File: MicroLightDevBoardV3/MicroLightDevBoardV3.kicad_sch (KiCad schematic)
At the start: 33 parts, among them J1 TYPE-C-31-M-12, J3 Conn_01x03_Socket, J4 Conn_01x01_Socket, J5 Conn_01x01_Socket, J6 Conn_01x04_Socket, SW1 SW_Push, U1 USBLC6-2P6, U2 STM32C071GBUx, U3 BQ25180, U4 S-85S1AB33-I6T1U, U7 MC3479

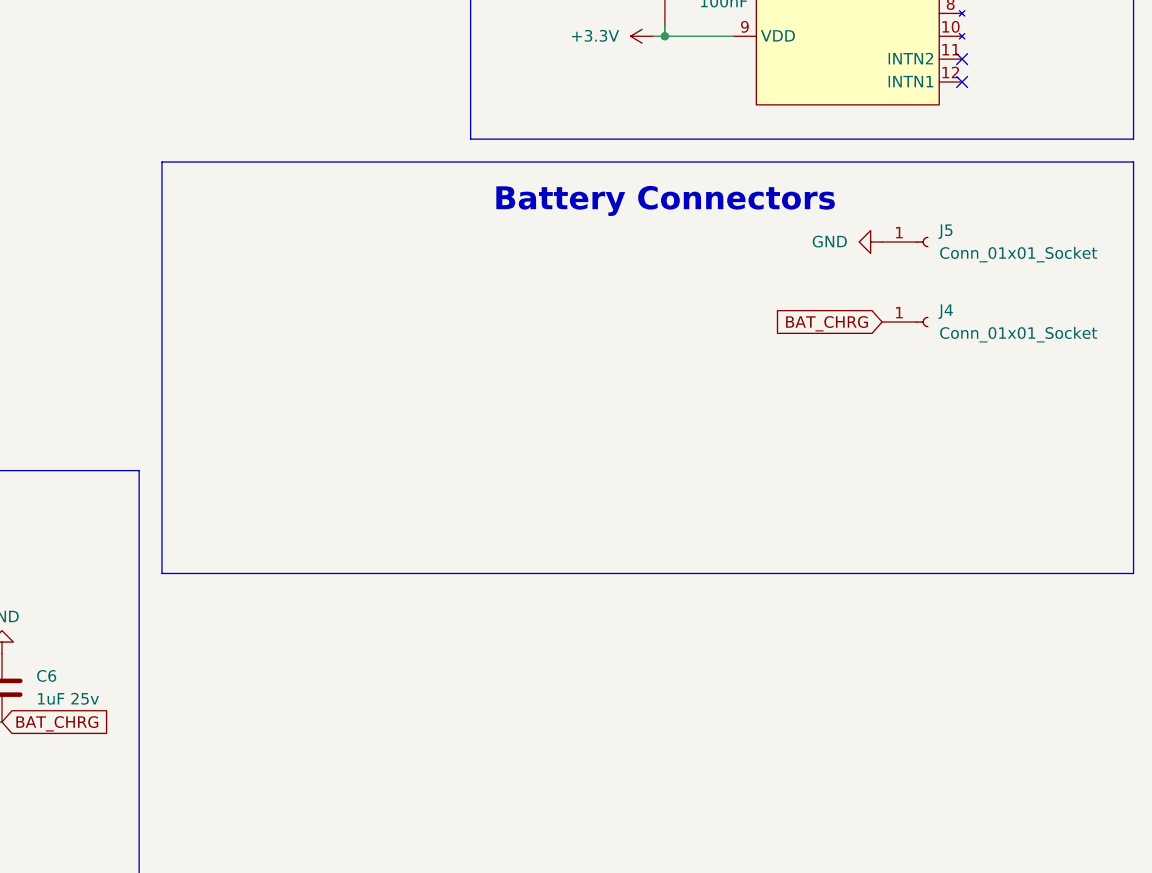
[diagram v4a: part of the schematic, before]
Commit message: add LCSC part numbers to schematic/pcb
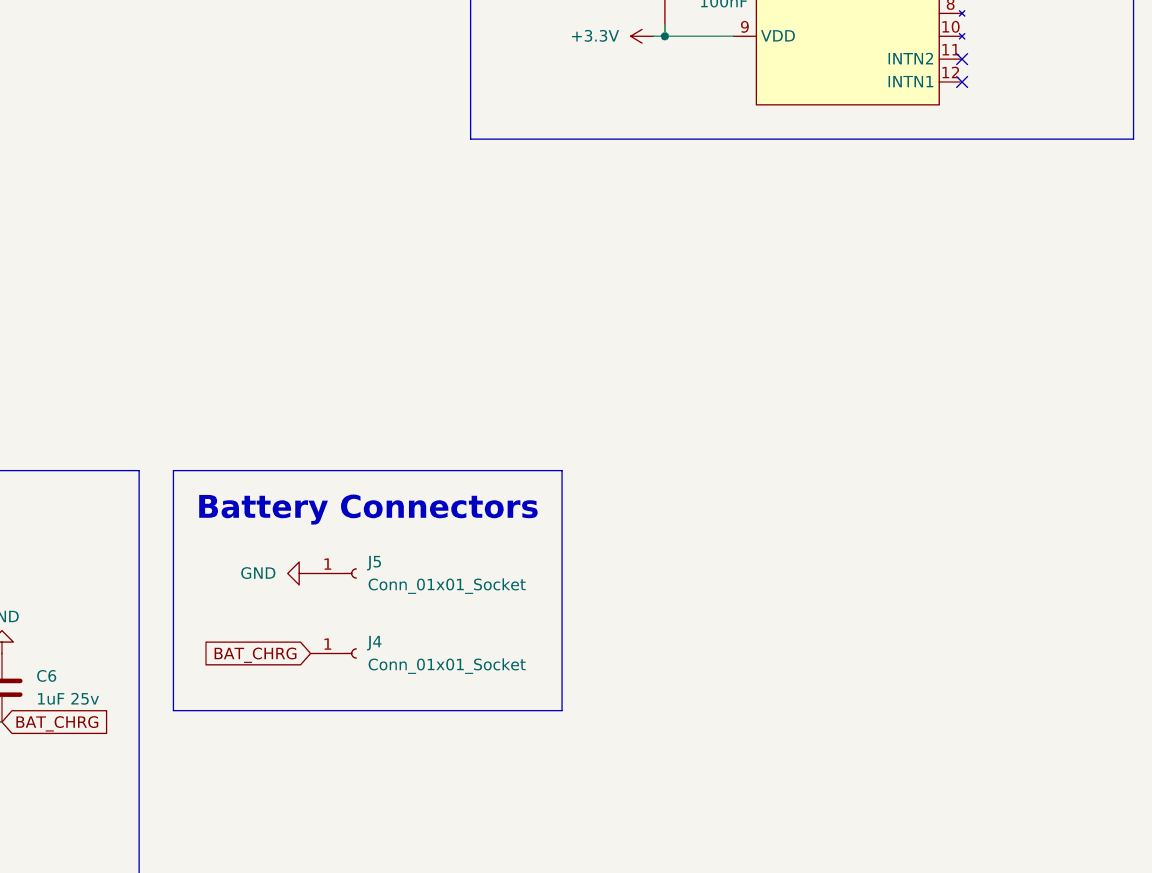
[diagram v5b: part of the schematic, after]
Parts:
- L1: LCSC (none) -> C92923; original_LCSC (none) -> C9900036204
- U4: LCSC (none) -> C7070110; LSCS C7070110 -> (none)
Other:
- moved on the sheet: J4, J5
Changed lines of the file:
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@@
 	)
 	(rectangle
-		(start 173.99 93.98)
-		(end 281.94 139.7)
+		(start 175.26 128.27)
+		(end 218.44 154.94)
 		(stroke
 			(width 0)
@@
 	(text "Battery Connectors"
 		(exclude_from_sim no)
-		(at 229.87 98.298 0)
+		(at 196.85 132.588 0)
 		(effects
 			(font
@@
 	(global_label "BAT_CHRG"
 		(shape input)
-		(at 254 111.76 180)
+		(at 190.5 148.59 180)
 		(fields_autoplaced yes)
 		(effects
@@
 		)
 		(property "Intersheetrefs" "${INTERSHEET_REFS}"
-			(at 241.5805 111.76 0)
+			(at 178.0805 148.59 0)
 			(effects
 				(font
@@
 	(symbol
 		(lib_id "Connector:Conn_01x01_Socket")
-		(at 259.08 111.76 0)
+		(at 195.58 148.59 0)
 		(unit 1)
 		(exclude_from_sim no)
@@
 		(fields_autoplaced yes)
 		(property "Reference" "J4"
-			(at 260.35 110.4899 0)
+			(at 196.85 147.3199 0)
 			(effects
 				(font
@@
 		)
 		(property "Value" "Conn_01x01_Socket"
-			(at 260.35 113.0299 0)
+			(at 196.85 149.8599 0)
 			(effects
 				(font
@@
 		)
 		(property "Footprint" "MicroLightDevBoard:battery_1x01_Vertical"
-			(at 259.08 111.76 0)
+			(at 195.58 148.59 0)
 			(effects
 				(font
@@
 		)
 		(property "Datasheet" "~"
-			(at 259.08 111.76 0)
+			(at 195.58 148.59 0)
 			(effects
 				(font
@@
 		)
 		(property "Description" "Generic connector, single row, 01x01, script generated"
-			(at 259.08 111.76 0)
+			(at 195.58 148.59 0)
 			(effects
 				(font
@@
 			)
 		)
-		(property "LSCS" "C7070110"
+		(property "LCSC" "C7070110"
 			(at 218.44 30.48 0)
 			(effects
@@
 	(symbol
 		(lib_id "Connector:Conn_01x01_Socket")
-		(at 259.08 102.87 0)
+		(at 195.58 139.7 0)
 		(unit 1)
 		(exclude_from_sim no)
@@
 		(fields_autoplaced yes)
 		(property "Reference" "J5"
-			(at 260.35 101.5999 0)
+			(at 196.85 138.4299 0)
 			(effects
 				(font
@@
 		)
 		(property "Value" "Conn_01x01_Socket"
-			(at 260.35 104.1399 0)
+			(at 196.85 140.9699 0)
 			(effects
 				(font
@@
 		)
 		(property "Footprint" "MicroLightDevBoard:battery_1x01_Vertical"
-			(at 259.08 102.87 0)
+			(at 195.58 139.7 0)
 			(effects
 				(font
@@
 		)
 		(property "Datasheet" "~"
-			(at 259.08 102.87 0)
+			(at 195.58 139.7 0)
 			(effects
 				(font
@@
 		)
 		(property "Description" "Generic connector, single row, 01x01, script generated"
-			(at 259.08 102.87 0)
+			(at 195.58 139.7 0)
 			(effects
 				(font
@@
 			)
 		)
+		(property "original_LCSC" "C9900036204"
+			(at 210.82 41.91 90)
+			(effects
+				(font
+					(size 1.27 1.27)
+				)
+				(hide yes)
+			)
+		)
+		(property "LCSC" "C92923"
+			(at 210.82 41.91 90)
+			(effects
+				(font
+					(size 1.27 1.27)
+				)
+				(hide yes)
+			)
+		)
 		(pin "2"
 		)
@@
 	(symbol
 		(lib_id "power:GND")
-		(at 254 102.87 270)
+		(at 190.5 139.7 270)
 		(unit 1)
 		(exclude_from_sim no)
@@
 		(fields_autoplaced yes)
 		(property "Reference" "#PWR024"
-			(at 247.65 102.87 0)
+			(at 184.15 139.7 0)
 			(effects
 				(font
@@
 		)
 		(property "Value" "GND"
-			(at 250.19 102.8699 90)
+			(at 186.69 139.6999 90)
 			(effects
 				(font
@@
 		)
 		(property "Footprint" ""
-			(at 254 102.87 0)
+			(at 190.5 139.7 0)
 			(effects
 				(font
@@
 		)
 		(property "Datasheet" ""
-			(at 254 102.87 0)
+			(at 190.5 139.7 0)
 			(effects
 				(font
@@
 		)
 		(property "Description" "Power symbol creates a global label with name \"GND\" , ground"
-			(at 254 102.87 0)
+			(at 190.5 139.7 0)
 			(effects
 				(font

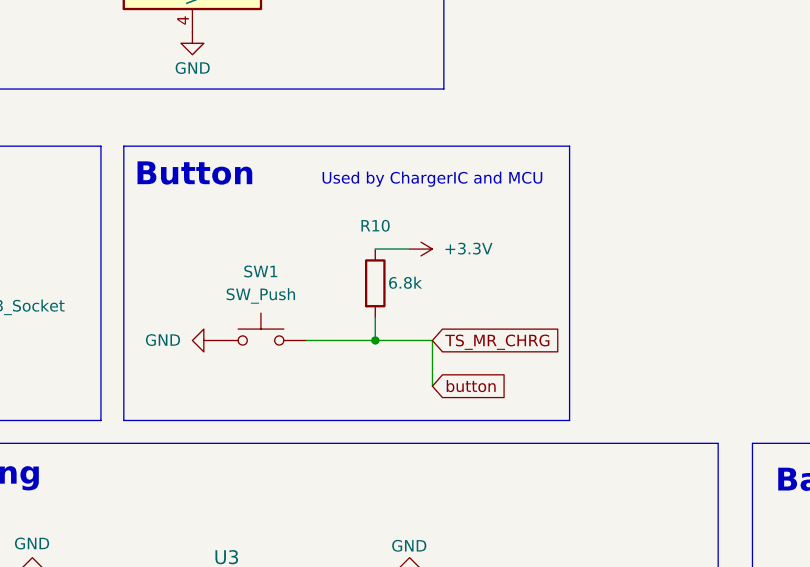
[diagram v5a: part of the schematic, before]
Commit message: update button pullup resistor value to value I (accidentally) actually used, it worked
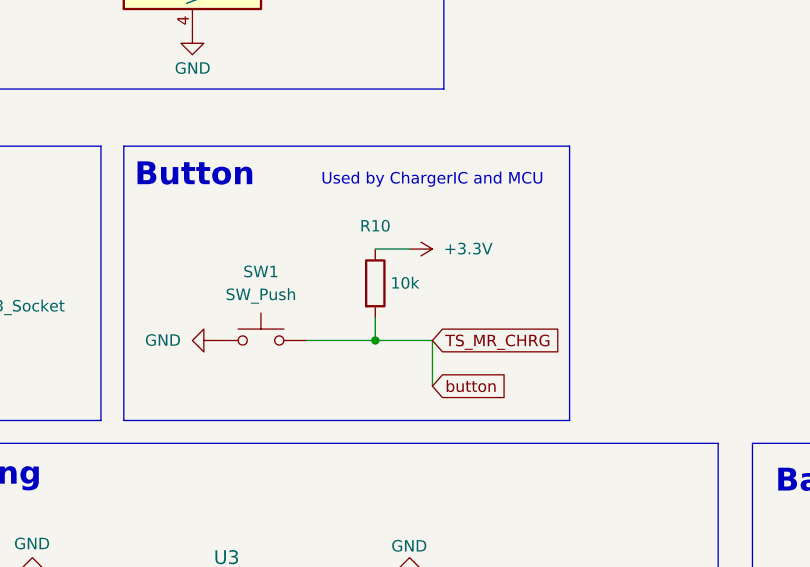
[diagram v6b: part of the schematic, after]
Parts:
- R10: value 6.8k -> 10k; LCSC (none) -> C25744
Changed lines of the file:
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@@
 			)
 		)
-		(property "Value" "6.8k"
+		(property "Value" "10k"
 			(at 136.652 110.49 0)
 			(effects
@@
 			(at 133.35 110.49 0)
 			(effects
+				(font
+					(size 1.27 1.27)
+				)
+				(hide yes)
+			)
+		)
+		(property "LCSC" "C25744"
+			(at 133.35 110.49 0)
+			(effects

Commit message: add LCSC part number for esd
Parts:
- U1: LCSC (none) -> C15999
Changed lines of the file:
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@@
+			)
+		)
+		(property "LCSC" "C15999"
+			(at 64.77 41.91 0)
+			(effects
+				(font
+					(size 1.27 1.27)
+				)
+				(hide yes)
 			)
 		)

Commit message: use cheap esd drop in replacement, disable usb peripherals when unplugged to save battery
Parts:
- U1: LCSC C15999 -> C3647099
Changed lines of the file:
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@@
 			)
 		)
-		(property "LCSC" "C15999"
+		(property "LCSC" "C3647099"
 			(at 64.77 41.91 0)
 			(effects
